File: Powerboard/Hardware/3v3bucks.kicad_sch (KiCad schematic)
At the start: 44 parts, among them IC1 SiC437BED-T1-GE3, IC2 SiC437BED-T1-GE3, Q5 SSM6J511NU,LF, Q6 SSM6J511NU,LF, U8 LTC4412xS6, U9 LTC4412xS6

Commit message: latest
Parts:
- removed 4.7uF1: 4.7uF, Capacitor_SMD:C_0402_1005Metric, symbol Device:C_Small
- removed C25, C26: C_Polarized_Small, Capacitor_SMD:CP_Elec_10x10, symbol Device:C_Polarized_Small
- removed C27: 100nF, symbol Device:C_Small
- removed C29, C31, C33, C35, C37: 10uF, Resistor_SMD:R_0805_2012Metric, symbol Device:C_Small
- removed C39: 47uF, Capacitor_SMD:CP_Elec_8x11.9, symbol Device:C_Polarized_Small
- removed C41: 0.1uF, Capacitor_SMD:C_0402_1005Metric, symbol Device:C_Small
- removed C43: 100nF, Resistor_SMD:R_1206_3216Metric, symbol Device:C_Small
- removed C45: 1uF, Capacitor_SMD:C_0402_1005Metric, symbol Device:C_Small
- removed IC1: SiC437BED-T1-GE3, iclr:SiC437BEDT1GE3, symbol iclr:SiC437BED-T1-GE3
- removed L3: 5.6uH, Inductor_SMD:L_6.3x6.3_H3, symbol pspice:INDUCTOR
- removed Q5, Q6: SSM6J511NU,LF, iclr:TRANS_SSM6J511NU,LF, symbol iclr:SSM6J511NU,LF
- removed R22: 45k, Resistor_SMD:R_0402_1005Metric, symbol Device:R_Small
- removed R23: 10k, Resistor_SMD:R_0402_1005Metric, symbol Device:R_Small
- removed R24: 100k, Resistor_SMD:R_0402_1005Metric, symbol Device:R_Small
- removed R26: 50k, Resistor_SMD:R_0402_1005Metric, symbol Device:R_Small
- removed R27: 2.2, Resistor_SMD:R_0402_1005Metric, symbol Device:R_Small
- removed R28: 499k, Resistor_SMD:R_0402_1005Metric, symbol Device:R_Small
- removed U9: LTC4412xS6, Package_TO_SOT_SMD:TSOT-23-6, symbol Power_Management:LTC4412xS6
- added C15, C25: 22uF, Capacitor_SMD:C_0603_1608Metric, symbol Device:C_Small
- added Q5, Q6: PXP012-30QLJ, iclr:PXP01230QLJ, symbol iclr:PXP012-30QLJ
- added U1: LTC4412xS6, Package_TO_SOT_SMD:TSOT-23-6, symbol Power_Management:LTC4412xS6
- C28: footprint (none) -> Capacitor_SMD:C_0402_1005Metric
- C30, C32, C34, C36, C38: value 10uF -> 22uF; footprint Resistor_SMD:R_0805_2012Metric -> Capacitor_SMD:C_0603_1608Metric
- C40: footprint Capacitor_SMD:CP_Elec_8x11.9 -> Capacitor_Tantalum_SMD:CP_EIA-7343-31_Kemet-D
- C44: footprint Resistor_SMD:R_1206_3216Metric -> Capacitor_SMD:C_0603_1608Metric
- L4: value 5.6uH -> 3.3uH; footprint Inductor_SMD:L_6.3x6.3_H3 -> Inductor_SMD:L_10.4x10.4_H4.8
- R31: value 499k -> 200k
- renumbered 4.7uF2 to C47
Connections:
- net GNDA is gone; now on net GND: C46.1, IC2.14 (P_GOOD), IC2.16 (A_GND), IC2.25 (AGND), R21.2, R31.2
- net +12V: now also Q5.1 (S_1), Q5.2 (S_2), Q5.3 (S_3), U1.1 (VIN); no longer C40.1, C44.1, IC2.1 (V_IN_1), IC2.2 (V_IN_2), IC2.22 (VIN_1), IC2.26 (VIN_2)
- net GND: now also C15.1, C25.1, U1.2 (GND), U1.3 (CTL)
- net at U8.5 (GATE): now also Q6.4 (G)
- net +3V3: no longer names the net of U8.6 (SENSE)
- net +3V3: now also C40.1, C44.1, IC2.1 (V_IN_1), IC2.2 (V_IN_2), IC2.22 (VIN_1), IC2.26 (VIN_2), Q5.5 (D_1), Q5.6 (D_2), Q5.7 (D_3), Q5.8 (D_4), Q5.9 (D_5), Q6.5 (D_1), Q6.6 (D_2), Q6.7 (D_3), Q6.8 (D_4), Q6.9 (D_5), U1.6 (SENSE)
- net BOOT1 renamed BOOT
- net FB1 renamed FB
- net MODE_1_1 renamed MODE_1
- net MODE_2_1 renamed MODE_2
- net PHASE1 renamed PHASE
- net STAT2 renamed USBPOWER
- net VOUT1 renamed RBUS_uC_V
- net RBUS_uC_V: now also C15.2, C25.2
- net VOUT2 renamed VBUS
- net VBUS: now also Q6.1 (S_1), Q6.2 (S_2), Q6.3 (S_3)
- net Vdd1 renamed Vdd
- new net: Q5.4 (G), U1.5 (GATE)
- new net LIPOPOWER: U1.4 (STAT)
- no-connect marks 8 -> 4
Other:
- note added: "Cmin = 100uF. Went for 22uF caps instead of 10uF to save space and lower ESR"
- note added: "SRP8540A-3R3M"
- note added: "Sim says up to 330uF on input for 12V, formulas suggest 20uF should suffice. N.B. formula uses Vcinpkpk of 500mV (upper bound)"
- note removed: "Wurth Elektronik 78439346056"
- moved on the sheet: C28, C30, C32, C34, C36, C38, C40, C42, C44, C46, C47, IC2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

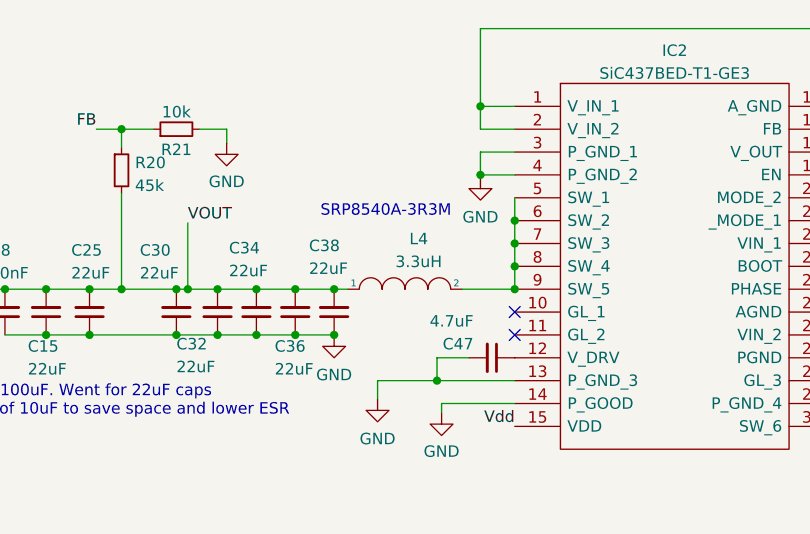
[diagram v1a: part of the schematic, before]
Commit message: i2c breakout, general clean up
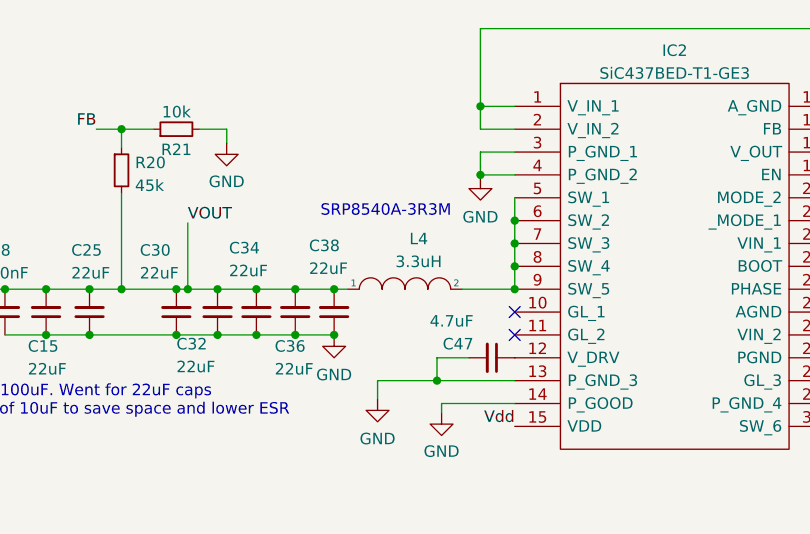
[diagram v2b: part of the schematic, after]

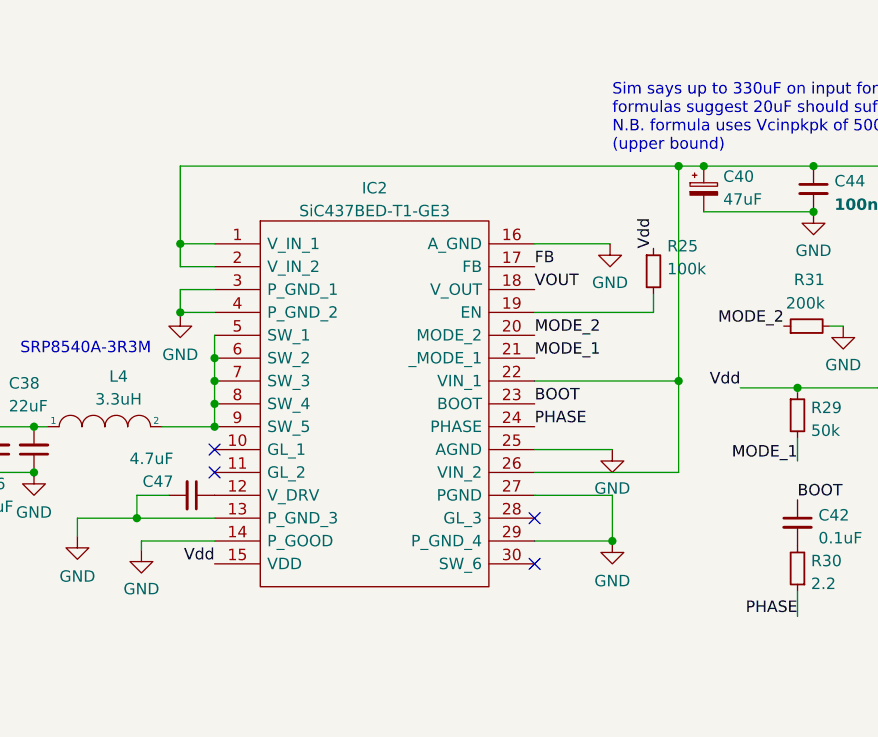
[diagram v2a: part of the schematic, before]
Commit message: vias fixed, ready for review
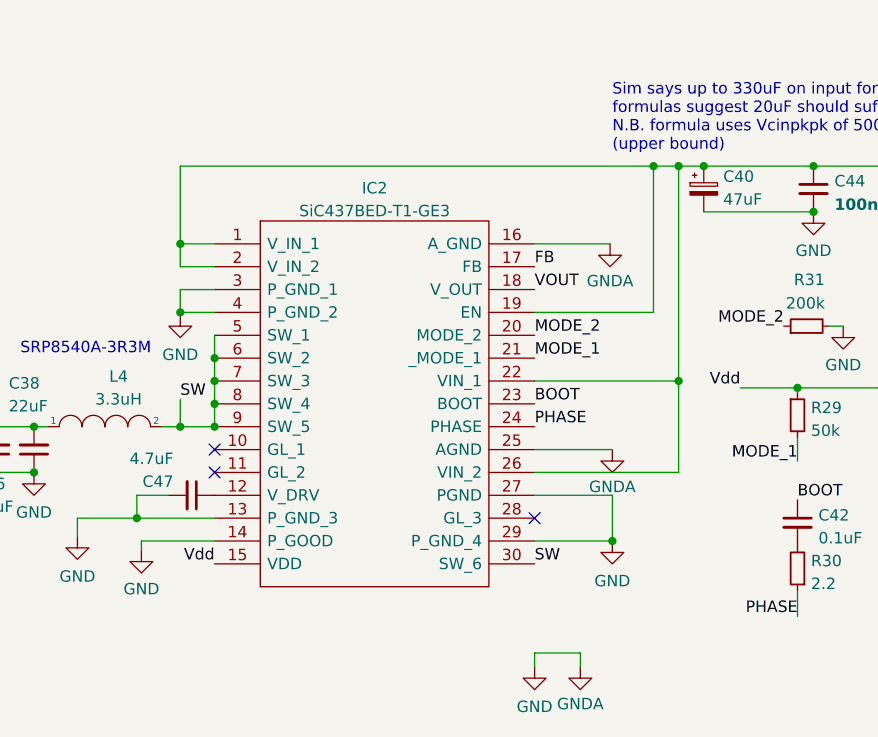
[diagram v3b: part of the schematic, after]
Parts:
- removed R25: 100k, Resistor_SMD:R_0402_1005Metric, symbol Device:R_Small
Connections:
- net at C40.1, C44.1, IC2.1 (V_IN_1)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: now also IC2.19 (EN)
- net SW: now reaches IC2.30 (SW_6)
- net SW: now also IC2.5 (SW_1), IC2.6 (SW_2), IC2.7 (SW_3), IC2.8 (SW_4), IC2.9 (SW_5), L4.2
- no-connect marks 4 -> 3
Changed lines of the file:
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@@
   (junction (at 226.568 52.578) (diameter 0) (color 0 0 0 0)
   )
+  (junction (at 111.506 112.268) (diameter 0) (color 0 0 0 0)
+  )
   (junction (at 63.246 112.268) (diameter 0) (color 0 0 0 0)
   )
@@
   (junction (at 260.858 50.038) (diameter 0) (color 0 0 0 0)
   )
+  (junction (at 164.084 83.312) (diameter 0) (color 0 0 0 0)
+  )
   (junction (at 266.954 52.578) (diameter 0) (color 0 0 0 0)
   )
@@
   )
   (no_connect (at 150.876 122.428))
-  (no_connect (at 150.876 127.508))
   (no_connect (at 115.316 114.808))
   (no_connect (at 115.316 117.348))
@@
     (stroke (width 0) (type default))
   )
+  (wire (pts (xy 164.084 83.312) (xy 164.084 99.568))
+    (stroke (width 0) (type default))
+  )
   (wire (pts (xy 78.994 112.268) (xy 82.296 112.268))
     (stroke (width 0) (type default))
@@
     (stroke (width 0) (type default))
   )
+  (wire (pts (xy 155.956 137.414) (xy 155.956 138.938))
+    (stroke (width 0) (type default))
+  )
   (wire (pts (xy 115.316 122.428) (xy 106.68 122.428))
     (stroke (width 0) (type default))
@@
     (stroke (width 0) (type default))
   )
+  (wire (pts (xy 150.876 137.414) (xy 155.956 137.414))
+    (stroke (width 0) (type default))
+  )
   (wire (pts (xy 166.878 83.312) (xy 169.672 83.312))
     (stroke (width 0) (type default))
@@
     (stroke (width 0) (type default))
   )
-  (wire (pts (xy 164.084 97.536) (xy 164.084 99.568))
-    (stroke (width 0) (type default))
-  )
   (wire (pts (xy 82.296 112.268) (xy 86.614 112.268))
     (stroke (width 0) (type default))
@@
     (stroke (width 0) (type default))
   )
-  (wire (pts (xy 111.506 83.312) (xy 166.878 83.312))
+  (wire (pts (xy 111.506 83.312) (xy 164.084 83.312))
     (stroke (width 0) (type default))
   )
@@
     (stroke (width 0) (type default))
   )
+  (wire (pts (xy 164.084 83.312) (xy 166.878 83.312))
+    (stroke (width 0) (type default))
+  )
   (wire (pts (xy 150.876 91.948) (xy 159.258 91.948))
     (stroke (width 0) (type default))
@@
     (stroke (width 0) (type default))
   )
+  (wire (pts (xy 150.876 138.938) (xy 150.876 137.414))
+    (stroke (width 0) (type default))
+  )
   (wire (pts (xy 226.568 52.578) (xy 235.458 52.578))
     (stroke (width 0) (type default))
@@
     (stroke (width 0) (type default))
   )
-  (wire (pts (xy 109.474 112.268) (xy 115.316 112.268))
+  (wire (pts (xy 109.474 112.268) (xy 111.506 112.268))
     (stroke (width 0) (type default))
   )
@@
     (stroke (width 0) (type default))
   )
+  (wire (pts (xy 111.506 109.22) (xy 111.506 112.268))
+    (stroke (width 0) (type default))
+  )
   (wire (pts (xy 78.994 104.902) (xy 78.994 112.268))
     (stroke (width 0) (type default))
@@
   )
   (wire (pts (xy 266.954 52.578) (xy 274.574 52.578))
+    (stroke (width 0) (type default))
+  )
+  (wire (pts (xy 111.506 112.268) (xy 115.316 112.268))
     (stroke (width 0) (type default))
   )
@@
     (effects (font (size 1.27 1.27)) (justify left bottom))
   )
+  (label "SW" (at 111.506 109.22 0) (fields_autoplaced)
+    (effects (font (size 1.27 1.27)) (justify left bottom))
+  )
   (label "PHASE" (at 180.086 133.35 180) (fields_autoplaced)
     (effects (font (size 1.27 1.27)) (justify right bottom))
@@
     (effects (font (size 1.27 1.27)) (justify left bottom))
   )
+  (label "SW" (at 150.876 127.508 0) (fields_autoplaced)
+    (effects (font (size 1.27 1.27)) (justify left bottom))
+  )
   (label "MODE_2" (at 178.562 101.092 180) (fields_autoplaced)
     (effects (font (size 1.27 1.27)) (justify right bottom))
@@
   (label "MODE_1" (at 180.086 116.078 180) (fields_autoplaced)
     (effects (font (size 1.27 1.27)) (justify right bottom))
-  )
-  (label "Vdd" (at 164.084 92.456 90) (fields_autoplaced)
-    (effects (font (size 1.27 1.27)) (justify left bottom))
   )
   (label "Vdd" (at 173.736 107.95 180) (fields_autoplaced)
@@
     )
   )
+  (symbol (lib_id "power:GNDA") (at 155.956 138.938 0) (unit 1)
+    (in_bom yes) (on_board yes) (dnp no) (fields_autoplaced)
+    (property "Reference" "#PWR04" (at 155.956 145.288 0)
+      (effects (font (size 1.27 1.27)) hide)
+    )
+    (property "Value" "GNDA" (at 155.956 143.0735 0)
+      (effects (font (size 1.27 1.27)))
+    )
+    (property "Footprint" "" (at 155.956 138.938 0)
+      (effects (font (size 1.27 1.27)) hide)
+    )
+    (property "Datasheet" "" (at 155.956 138.938 0)
+      (effects (font (size 1.27 1.27)) hide)
+    )
+    (pin "1")
+    (instances
+      (project "Switcher"
+        (path "/e63e39d7-6ac0-4ffd-8aa3-1841a4541b55/e469982c-3823-4665-9e6d-e90b00c2da09"
+          (reference "#PWR04") (unit 1)
+        )
+      )
+    )
+  )
   (symbol (lib_id "power:GND") (at 198.12 109.728 0) (unit 1)
     (in_bom yes) (on_board yes) (dnp no)
@@
     )
   )
-  (symbol (lib_id "power:GND") (at 159.258 91.948 0) (unit 1)
-    (in_bom yes) (on_board yes) (dnp no)
-    (property "Reference" "#PWR0164" (at 159.258 98.298 0)
-      (effects (font (size 1.27 1.27)) hide)
-    )
-    (property "Value" "GND" (at 159.258 96.266 0)
-      (effects (font (size 1.27 1.27)))
-    )
-    (property "Footprint" "" (at 159.258 91.948 0)
-      (effects (font (size 1.27 1.27)) hide)
-    )
-    (property "Datasheet" "" (at 159.258 91.948 0)
-      (effects (font (size 1.27 1.27)) hide)
-    )
-    (pin "1")
-    (instances
-      (project "Switcher"
-        (path "/e63e39d7-6ac0-4ffd-8aa3-1841a4541b55/e469982c-3823-4665-9e6d-e90b00c2da09"
-          (reference "#PWR0164") (unit 1)
-        )
-      )
-    )
-  )
-  (symbol (lib_id "Device:R_Small") (at 164.084 94.996 0) (unit 1)
-    (in_bom yes) (on_board yes) (dnp no)
-    (property "Reference" "R25" (at 165.608 92.2051 0)
-      (effects (font (size 1.27 1.27)) (justify left))
-    )
-    (property "Value" "100k" (at 165.608 94.742 0)
-      (effects (font (size 1.27 1.27)) (justify left))
-    )
-    (property "Footprint" "Resistor_SMD:R_0402_1005Metric" (at 164.084 94.996 0)
-      (effects (font (size 1.27 1.27)) hide)
-    )
-    (property "Datasheet" "~" (at 164.084 94.996 0)
-      (effects (font (size 1.27 1.27)) hide)
-    )
-    (pin "1")
-    (pin "2")
-    (instances
-      (project "Switcher"
-        (path "/e63e39d7-6ac0-4ffd-8aa3-1841a4541b55/e469982c-3823-4665-9e6d-e90b00c2da09"
-          (reference "R25") (unit 1)
-        )
-      )
-    )
-  )
   (symbol (lib_id "Device:C_Polarized_Small") (at 169.672 85.852 0) (unit 1)
     (in_bom yes) (on_board yes) (dnp no) (fields_autoplaced)
@@
         (path "/e63e39d7-6ac0-4ffd-8aa3-1841a4541b55/e469982c-3823-4665-9e6d-e90b00c2da09"
           (reference "C40") (unit 1)
-        )
-      )
-    )
-  )
-  (symbol (lib_id "power:GND") (at 159.512 114.808 0) (unit 1)
-    (in_bom yes) (on_board yes) (dnp no)
-    (property "Reference" "#PWR0163" (at 159.512 121.158 0)
-      (effects (font (size 1.27 1.27)) hide)
-    )
-    (property "Value" "GND" (at 159.512 119.126 0)
-      (effects (font (size 1.27 1.27)))
-    )
-    (property "Footprint" "" (at 159.512 114.808 0)
-      (effects (font (size 1.27 1.27)) hide)
-    )
-    (property "Datasheet" "" (at 159.512 114.808 0)
-      (effects (font (size 1.27 1.27)) hide)
-    )
-    (pin "1")
-    (instances
-      (project "Switcher"
-        (path "/e63e39d7-6ac0-4ffd-8aa3-1841a4541b55/e469982c-3823-4665-9e6d-e90b00c2da09"
-          (reference "#PWR0163") (unit 1)
         )
       )
@@
     )
   )
+  (symbol (lib_id "power:GND") (at 150.876 138.938 0) (unit 1)
+    (in_bom yes) (on_board yes) (dnp no) (fields_autoplaced)
+    (property "Reference" "#PWR05" (at 150.876 145.288 0)
+      (effects (font (size 1.27 1.27)) hide)
+    )
+    (property "Value" "GND" (at 150.876 143.3814 0)
+      (effects (font (size 1.27 1.27)))
+    )
+    (property "Footprint" "" (at 150.876 138.938 0)
+      (effects (font (size 1.27 1.27)) hide)
+    )
+    (property "Datasheet" "" (at 150.876 138.938 0)
+      (effects (font (size 1.27 1.27)) hide)
+    )
+    (pin "1")
+    (instances
+      (project "Switcher"
+        (path "/e63e39d7-6ac0-4ffd-8aa3-1841a4541b55/e469982c-3823-4665-9e6d-e90b00c2da09"
+          (reference "#PWR05") (unit 1)
+        )
+      )
+    )
+  )
+  (symbol (lib_id "power:GNDA") (at 159.512 114.808 0) (unit 1)
+    (in_bom yes) (on_board yes) (dnp no) (fields_autoplaced)
+    (property "Reference" "#PWR02" (at 159.512 121.158 0)
+      (effects (font (size 1.27 1.27)) hide)
+    )
+    (property "Value" "GNDA" (at 159.512 118.9435 0)
+      (effects (font (size 1.27 1.27)))
+    )
+    (property "Footprint" "" (at 159.512 114.808 0)
+      (effects (font (size 1.27 1.27)) hide)
+    )
+    (property "Datasheet" "" (at 159.512 114.808 0)
+      (effects (font (size 1.27 1.27)) hide)
+    )
+    (pin "1")
+    (instances
+      (project "Switcher"
+        (path "/e63e39d7-6ac0-4ffd-8aa3-1841a4541b55/e469982c-3823-4665-9e6d-e90b00c2da09"
+          (reference "#PWR02") (unit 1)
+        )
+      )
+    )
+  )
   (symbol (lib_id "Device:C_Small") (at 63.246 114.808 180) (unit 1)
     (in_bom yes) (on_board yes) (dnp no)
@@
         )
       )
+    )
+  )
+  (symbol (lib_id "power:GNDA") (at 159.258 91.948 0) (unit 1)
+    (in_bom yes) (on_board yes) (dnp no) (fields_autoplaced)
+    (property "Reference" "#PWR03" (at 159.258 98.298 0)
+      (effects (font (size 1.27 1.27)) hide)
+    )
+    (property "Value" "GNDA" (at 159.258 96.0835 0)
+      (effects (font (size 1.27 1.27)))
+    )
+    (property "Footprint" "" (at 159.258 91.948 0)
+      (effects (font (size 1.27 1.27)) hide)
+    )
+    (property "Datasheet" "" (at 159.258 91.948 0)
+      (effects (font (size 1.27 1.27)) hide)
+    )
+    (pin "1")
+    (instances
+      (project "Switcher"
+        (path "/e63e39d7-6ac0-4ffd-8aa3-1841a4541b55/e469982c-3823-4665-9e6d-e90b00c2da09"
+          (reference "#PWR03") (unit 1)
+        )
+      )

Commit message: kiran/andrei review
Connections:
- net +12V: now also Q5.5 (D_1), Q5.6 (D_2), Q5.7 (D_3), Q5.8 (D_4), Q5.9 (D_5); no longer Q5.1 (S_1), Q5.2 (S_2), Q5.3 (S_3)
- net VBUS: now also Q6.5 (D_1), Q6.6 (D_2), Q6.7 (D_3), Q6.8 (D_4), Q6.9 (D_5); no longer Q6.1 (S_1), Q6.2 (S_2), Q6.3 (S_3)
- new net: C40.1, C44.1, IC2.1 (V_IN_1), IC2.19 (EN), IC2.2 (V_IN_2), IC2.22 (VIN_1), IC2.26 (VIN_2), Q5.1 (S_1), Q5.2 (S_2), Q5.3 (S_3), Q6.1 (S_1), Q6.2 (S_2), Q6.3 (S_3), U1.6 (SENSE), U8.6 (SENSE)
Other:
- moved on the sheet: Q5, Q6
